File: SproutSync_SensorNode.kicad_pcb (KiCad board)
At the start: 2 copper layers, 32.5 x 70.2 mm, 83 parts, among them J1 S2B-PH-K-S, J2 BM04B-SRSS-TB, J3 OSTVN04A150, J4 10132797-031100LF, J5 10132797-031100LF, J6 OSTVN02A150, J7 Conn_01x03, Q2 SSM3J35MFV, Q3 SSM3K16FV, U11 DRV8838DSGR, U2 TPS22914BYFPR, U3 TPS22914BYFPR, U4 SN65HVD3082EDR, U5 TXB0104RGYR, U6 TPS629203DRL, U7 BME688, U8 TPS22914BYFPR, U9 TPS629206DRLR

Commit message: ver2 layout in progress
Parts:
- removed C13, C14: 1uF, Capacitor_SMD:C_0402_1005Metric
- removed D1, D2, D3: DESD5V0S1BA-7, Diode_SMD:D_SOD-323
- removed R18, R4, R5: 4.7k, Resistor_SMD:R_0402_1005Metric
- removed the REF** at (98.8, 127.7)
- removed the REF** at (117.5, 120.5)
- added C2: 1uF, Capacitor_SMD:C_0402_1005Metric, F.Cu at (87.4, 80.3)
- added C22: 1uF, Capacitor_SMD:C_0402_1005Metric, F.Cu at (90.1, 78.5)
- added C23: 1uF, Capacitor_SMD:C_0402_1005Metric, F.Cu at (93.9, 80.3)
- added C24: 1uF, Capacitor_SMD:C_0402_1005Metric, F.Cu at (96.7, 78.7)
- added D7: B2841USD, LED_SMD:LED_0402_1005Metric, F.Cu at (84.3, 49.5)
- added J8: Conn_ARM_JTAG_SWD_10, Connector_PinHeader_1.27mm:PinHeader_2x05_P1.27mm_Vertical_SMD, F.Cu at (79.0, 78.5)
- added R11: 4.7k, Resistor_SMD:R_0402_1005Metric, F.Cu at (81.2, 74.0)
- added R12: 0, Resistor_SMD:R_0402_1005Metric, F.Cu at (92.2, 96.8)
- added R14: 4.7k, Resistor_SMD:R_0402_1005Metric, F.Cu at (76.2, 30.7)
- added R9: 1k, Resistor_SMD:R_0402_1005Metric, F.Cu at (84.3, 50.5)
- added REF**: MountingHole_2.5mm, MountingHole:MountingHole_2.5mm, F.Cu at (77.5, 70.5)
- added REF**: MountingHole_2.5mm, MountingHole:MountingHole_2.5mm, F.Cu at (98.8, 102.2)
- added TP12: TestPoint, TestPoint:TestPoint_Pad_D1.0mm, F.Cu at (66.2, 92.5)
- added TP5: TestPoint, TestPoint:TestPoint_Pad_D1.0mm, F.Cu at (66.2, 89.5)
- added U10: SN74LVC1T45DBVR, SproutSenseFootprints:SOT95P280X145-6N, F.Cu at (90.1, 80.8)
- added U12: SN74LVC1T45DBVR, SproutSenseFootprints:SOT95P280X145-6N, F.Cu at (96.7, 80.9)
- added U13: TL3305AF260QG, SproutSenseFootprints:SW_TL3305AF260QG, F.Cu at (90.5, 51.1)
- added U14: CDSOT23-SM712, SproutSenseFootprints:SOT_SM712, F.Cu at (93.3, 93.9)
- U5: value TXB0104RGYR -> TL3305AF260QG; footprint SproutSenseFootprints:QFN50P350X350X100-15N -> SproutSenseFootprints:SW_TL3305AF260QG
- moved TP3 60.2 mm to (43.5, 96.2)
- moved TP4 59.8 mm to (41.0, 95.7)
- moved TP11 54.4 mm to (66.6, 100.5)
- moved TP14 54.4 mm to (66.6, 105.3)
- moved TP15 54.4 mm to (66.6, 107.7)
- moved TP7 54.4 mm to (66.6, 98.1)
- moved TP8 54.4 mm to (66.6, 102.9)
- moved TP9 54.4 mm to (55.2, 99.0)
- moved TP10 54.4 mm to (52.6, 99.0)
- moved R2 53.1 mm to (58.2, 87.3), turned to 0 degrees
- moved D4 51.6 mm to (58.2, 88.4), turned to 0 degrees
- moved D5 50.3 mm to (58.2, 89.5), turned to 0 degrees
- moved R6 49.0 mm to (58.2, 90.5), turned to 0 degrees
- moved C4 31.8 mm to (88.5, 86.6)
- moved C6 31.8 mm to (88.5, 88.5)
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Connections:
- net /LEDIndicators/LORA_TX renamed /PetalStackingConectors/LORA_TX
- C8 pad 1: +5V -> SOIL_PWR_5p0
- J4 pad 1: unconnected-(J4-Pad1) -> /PetalStackingConectors/PAD0
- J4 pad 20: unconnected-(J4-Pad20) -> /PetalStackingConectors/PAD6
- J4 pad 22: unconnected-(J4-Pad22) -> /PetalStackingConectors/PAD8
- J4 pad 23: unconnected-(J4-Pad23) -> /PetalStackingConectors/PAD37
- J4 pad 25: unconnected-(J4-Pad25) -> /PetalStackingConectors/PAD10
- J4 pad 26: unconnected-(J4-Pad26) -> /PetalStackingConectors/PAD9
- J4 pad 27: unconnected-(J4-Pad27) -> /DebugProbe/nRESET
- J4 pad 28: unconnected-(J4-Pad28) -> /PetalStackingConectors/PAD20
- J4 pad 3: unconnected-(J4-Pad3) -> /PetalStackingConectors/PAD23
- J4 pad 4: unconnected-(J4-Pad4) -> /PetalStackingConectors/PAD24
- J4 pad 5: unconnected-(J4-Pad5) -> /PetalStackingConectors/PAD26
- J4 pad 6: unconnected-(J4-Pad6) -> /PetalStackingConectors/PAD21
- J4 pad 8: unconnected-(J4-Pad8) -> /PetalStackingConectors/PAD25
- J4 pad 9: unconnected-(J4-Pad9) -> /PetalStackingConectors/PAD5
- J7 pad 1: /PetalStackingConectors/PAD14 -> /PetalStackingConectors/PAD5
- R3 pad 1: RS485_A+ -> RS485_B-
- R3 pad 2: RS485_B- -> Net-(R12-Pad1)
- TP1 pad 1: /PetalStackingConectors/PAD31 -> /PetalStackingConectors/PAD15
- TP2 pad 1: /PetalStackingConectors/PAD30 -> /PetalStackingConectors/PAD14
- U11 pad 5: /PetalStackingConectors/PAD13 -> /PetalStackingConectors/PAD4
- U11 pad 6: /PetalStackingConectors/PAD12 -> /PetalStackingConectors/PAD2
- U4 pad 2: RE/DE -> /PetalStackingConectors/PAD1
- U4 pad 3: RE/DE -> /PetalStackingConectors/PAD1
- U4 pad 8: +5V -> SOIL_PWR_5p0
- U5 pad 1: +3V3 -> /DebugProbe/nRESET
- U5 pad 2: /PetalStackingConectors/PAD30 -> /DebugProbe/nRESET
- U5 pad 3: /PetalStackingConectors/PAD31 -> GND
- U5 pad 4: /PetalStackingConectors/PAD1 -> GND
- U8 pad B2: /PetalStackingConectors/PAD15 -> /PetalStackingConectors/PAD6
- U9 pad 7: /PetalStackingConectors/PAD35 -> /PetalStackingConectors/PAD8
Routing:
- net /PetalStackingConectors/PAD13: track 53.6 -> 0.00 mm, vias 2 -> 0
- net /PetalStackingConectors/PAD15: track 52.8 -> 0.00 mm, vias 2 -> 0
- net +5V: track 85.4 -> 33.4 mm, vias 15 -> 8
- net /PetalStackingConectors/PAD12: track 51.3 -> 0.00 mm, vias 2 -> 1
- net /PetalStackingConectors/PAD29: track 45.0 -> 0.00 mm, vias 2 -> 0
- net /PetalStackingConectors/PAD14: track 42.3 -> 0.00 mm, vias 1 -> 0
- net /PetalStackingConectors/PAD7: track 41.9 -> 0.00 mm, vias 2 -> 0
- net +3V3: track 77.4 -> 36.7 mm, vias 7 -> 8
- net /PetalStackingConectors/PAD30: track 37.0 -> 0.00 mm, vias 2 -> 0
- net /PetalStackingConectors/PAD35: track 35.0 -> 0.00 mm, vias 2 -> 0
- net AMB_PWR_3p3: track 14.3 -> 47.4 mm, vias 0 -> 4
- net TX: track 28.8 -> 3.83 mm, vias 2 -> 0
- net /PetalStackingConectors/PAD1: track 24.9 -> 0.00 mm, vias 2 -> 1
- net /PetalStackingConectors/PAD31: track 23.3 -> 0.00 mm, vias 2 -> 1
- net /PetalStackingConectors/PAD48: track 37.4 -> 15.6 mm, vias 3 -> 0
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- added copper zone on B.Cu, net AMB_PWR_3p3
- added copper zone on F.Cu, net AMB_PWR_3p3
- added copper zone on B.Cu, net IRRI_PWR_5p0
- added copper zone on F.Cu, net IRRI_PWR_5p0
- added copper zone on B.Cu, net SOIL_PWR_5p0
- added copper zone on F.Cu, net SOIL_PWR_5p0
- removed copper zone on B.Cu, net GND
- removed copper zone on F.Cu, net GND
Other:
- board size 32.5 x 70.2 mm -> 87.8 x 68.4 mm
- board text removed: "3.3V"
- board text removed: "5V"
- board text removed: "5V|B-|A+|GND"
- board text removed: "5V|GND"
- board text removed: "A"
- board text removed: "A+"
- board text removed: "B-"
- board text removed: "GND"
- board text removed: "GND|BAT+"
- board text removed: "SCL"
- board text removed: "SDA"
- board text removed: "SNS+"
- board text removed: "SNS-"

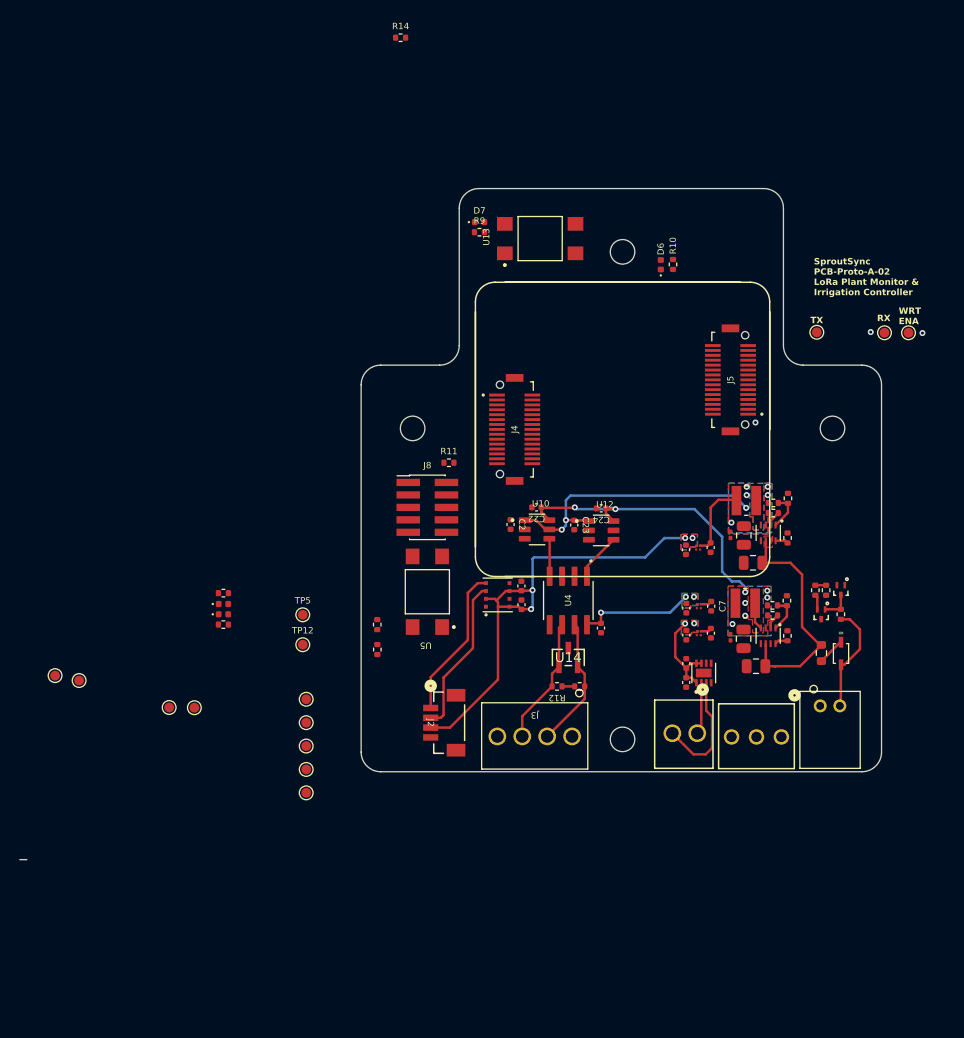
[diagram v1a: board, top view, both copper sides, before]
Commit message: rev2 precheck DRC clean
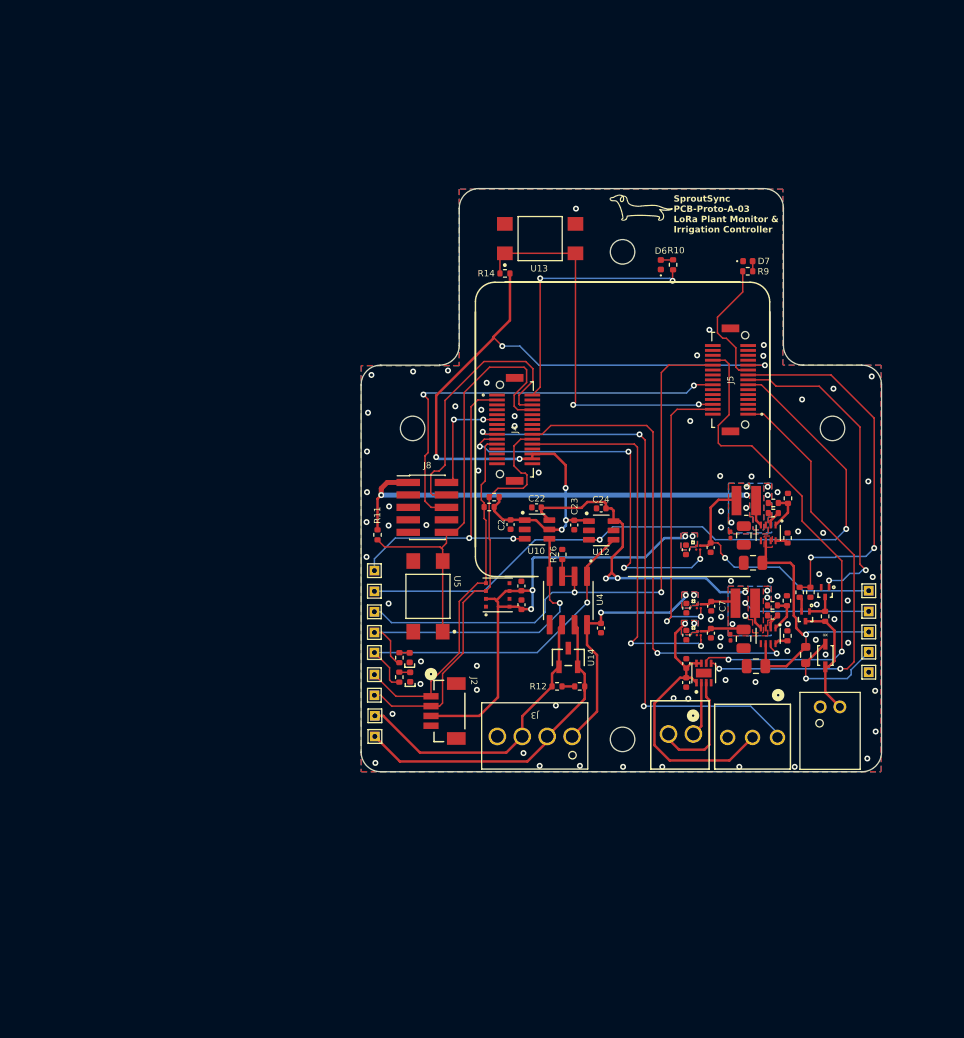
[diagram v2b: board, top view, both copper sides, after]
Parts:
- added G***: LOGO, TeenieWeenieLibrary:TeenieWeenieLogo, F.Cu at (100.8, 48.3)
- added R26: 9.31k, Resistor_SMD:R_0402_1005Metric, F.Cu at (92.7, 83.3)
- R7: value 7.5k -> 20k
- TP1, TP10, TP11, TP12, TP14, TP15, TP2, TP3, TP4, TP5, TP6, TP7, TP8, TP9: footprint TestPoint:TestPoint_Pad_D1.0mm -> TestPoint:TestPoint_THTPad_1.0x1.0mm_Drill0.5mm
- moved TP6 61.4 mm to (73.5, 89.2)
- moved TP15 60.3 mm to (124.0, 89.2), turned to -90 degrees
- moved TP14 60.2 mm to (124.0, 87.0), turned to -90 degrees
- moved TP1 58.3 mm to (73.5, 87.1)
- moved TP8 58.1 mm to (124.0, 93.3)
- moved TP11 58.1 mm to (124.0, 91.2)
- moved TP7 57.4 mm to (124.0, 95.3)
- moved TP2 51.2 mm to (73.5, 85.0)
- moved TP4 32.9 mm to (73.6, 99.8)
- moved TP3 30.7 mm to (73.6, 101.9)
- moved D7 27.6 mm to (111.6, 53.5)
- moved R9 27.6 mm to (111.6, 54.5)
- moved R14 26.3 mm to (86.9, 54.7)
- moved TP10 21.2 mm to (73.5, 95.6)
- moved D4 20.4 mm to (77.2, 95.8), turned to 90 degrees
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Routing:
- net +3V3: track 36.7 -> 156.3 mm, vias 8 -> 15
- net /PetalStackingConectors/PAD15: track 0.00 -> 72.5 mm, vias 0 -> 2
- net /PetalStackingConectors/PAD1: track 0.00 -> 64.4 mm, vias 1 -> 2
- net /PetalStackingConectors/PAD5: track 0.00 -> 61.0 mm, vias 0 -> 3
- net /PetalStackingConectors/PAD2: track 0.00 -> 53.3 mm, vias 0 -> 2
- net /PetalStackingConectors/PAD8: track 0.00 -> 49.1 mm, vias 0 -> 2
- net /DebugProbe/nRESET: track 0.00 -> 46.5 mm
- net /PetalStackingConectors/PAD4: track 0.00 -> 45.8 mm, vias 0 -> 2
- net /PetalStackingConectors/PAD41: track 0.00 -> 43.6 mm, vias 0 -> 2
- net /PetalStackingConectors/PAD6: track 0.00 -> 39.5 mm, vias 0 -> 2
- net /PetalStackingConectors/PAD16: track 0.00 -> 39.3 mm, vias 0 -> 2
- net /PetalStackingConectors/PAD7: track 0.00 -> 39.0 mm, vias 0 -> 4
- net /PetalStackingConectors/PAD33: track 1.10 -> 38.9 mm, vias 0 -> 2
- net /PetalStackingConectors/PAD14: track 0.00 -> 33.8 mm, vias 0 -> 2
- net /PetalStackingConectors/PAD32: track 0.00 -> 33.1 mm, vias 0 -> 2
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- added copper zone on B.Cu, net GND
- added copper zone on F.Cu, net GND
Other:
- board size 87.8 x 68.4 mm -> 53 x 59.5 mm
- board text added: "SproutSync PCB-Proto-A-03 LoRa Plant Monitor & Irrigation Controller"
- board text removed: "RX"
- board text removed: "SproutSync PCB-Proto-A-02 LoRa Plant Monitor & Irrigation Controller"
- board text removed: "TX"
- board text removed: "WRT ENA"

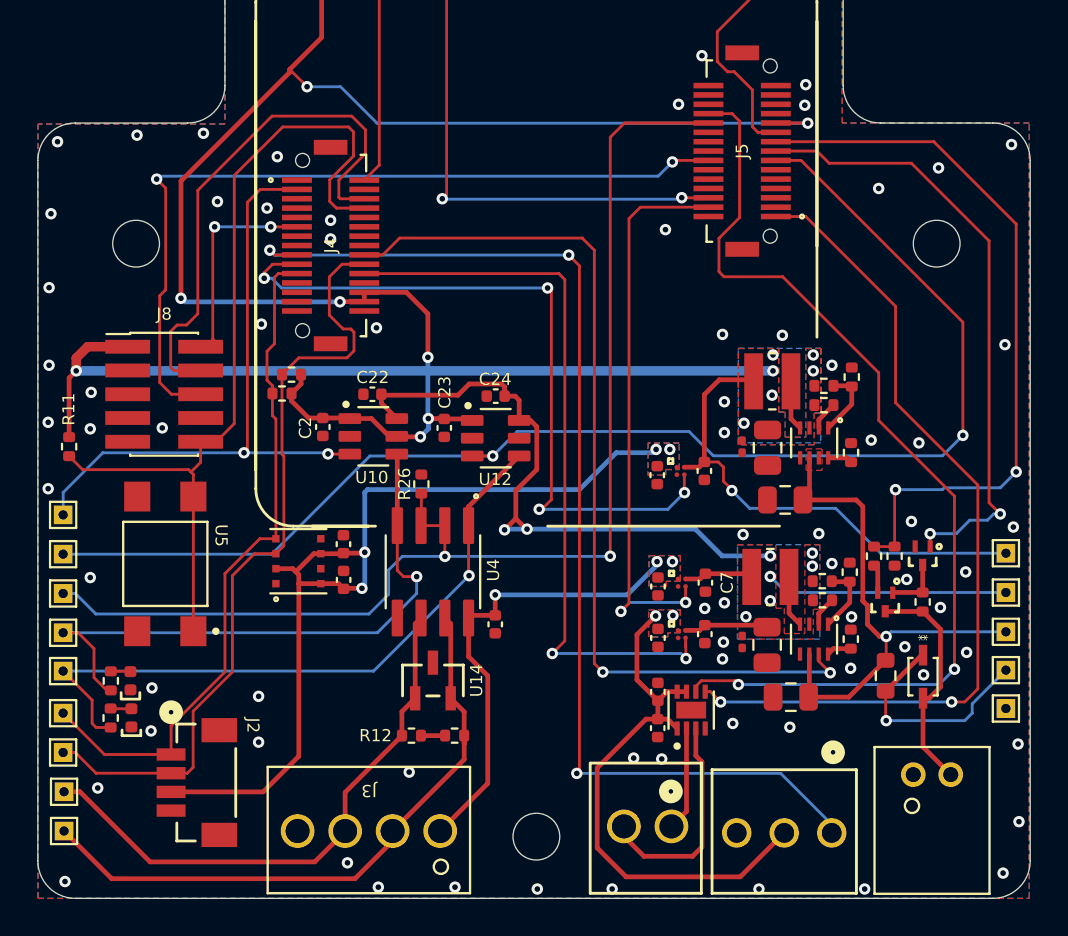
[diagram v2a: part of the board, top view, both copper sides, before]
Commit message: add diode cathode indicator
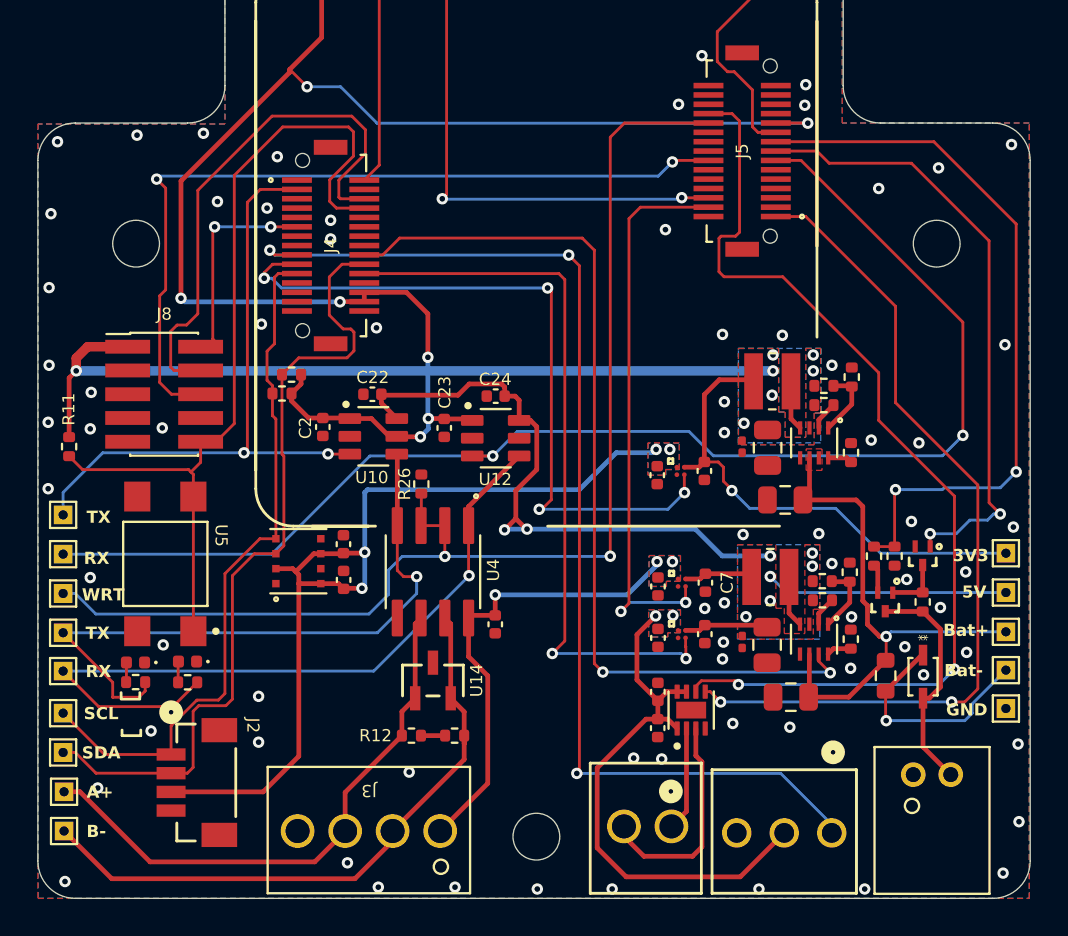
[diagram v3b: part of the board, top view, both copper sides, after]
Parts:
- moved R2 4.54 mm to (80.2, 94.0), turned to 180 degrees
- moved D4 4.25 mm to (80.2, 92.8), turned to 180 degrees
- moved R6 1.33 mm to (77.4, 93.9), turned to 180 degrees
- moved D5 1.01 mm to (77.4, 92.9), turned to 180 degrees
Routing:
- net RX: track 35.9 -> 39.8 mm
- net TX: track 32.8 -> 35.0 mm
- net /PetalStackingConectors/PAD49: track 42.5 -> 43.4 mm
- net /PetalStackingConectors/PAD48: track 36.7 -> 37.3 mm
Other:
- board text added: "3V3"
- board text added: "5V"
- board text added: "A+"
- board text added: "B-"
- board text added: "Bat+"
- board text added: "Bat-"
- board text added: "GND"
- board text added: "RX"
- board text added: "SCL"
- board text added: "SDA"
- board text added: "TX"
- board text added: "WRT"
